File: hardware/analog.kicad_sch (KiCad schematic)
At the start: 23 parts

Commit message: updated trig
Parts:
- renumbered C5 to C?, C6 to C?, C4 to C?, C3 to C?

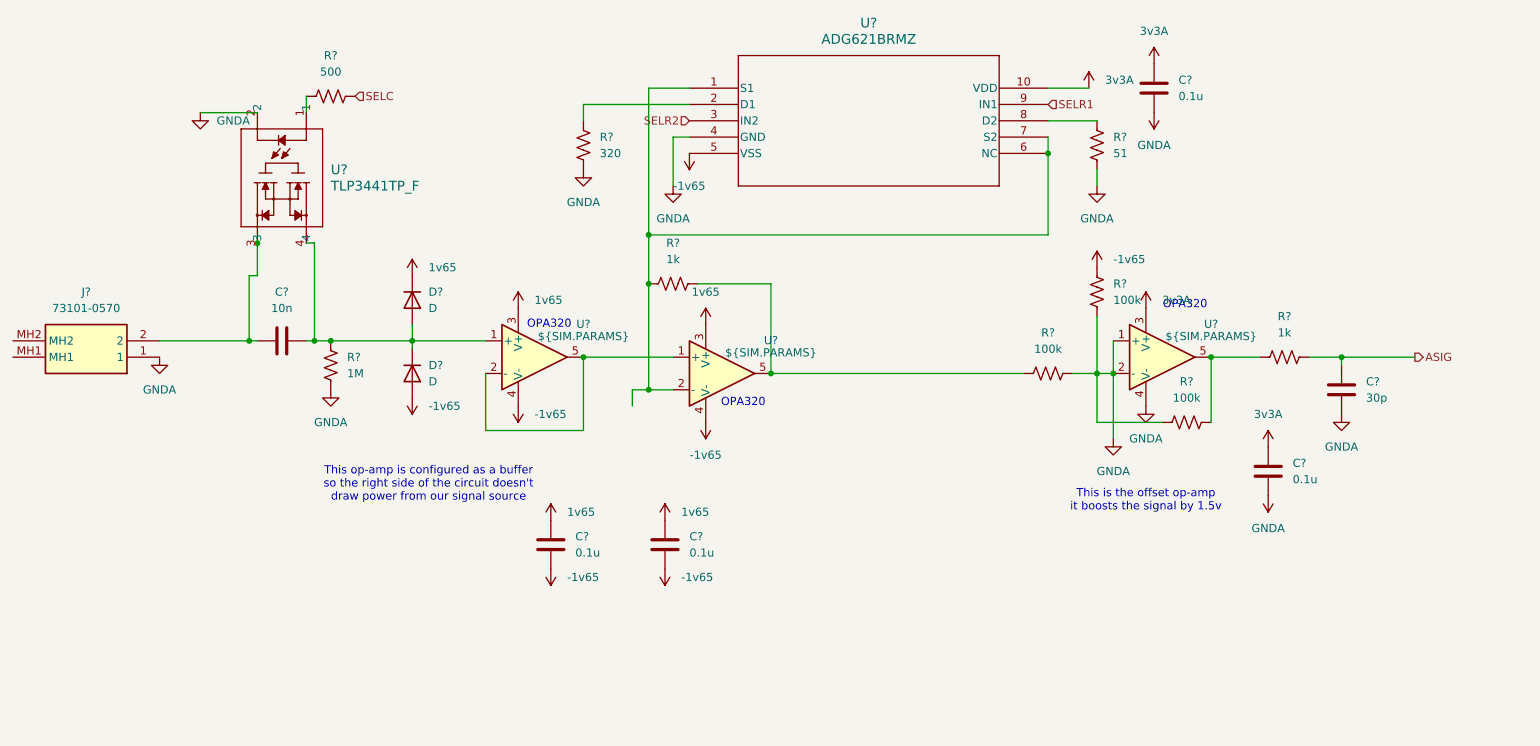
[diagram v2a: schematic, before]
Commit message: feat(hardware): Cleanup schematic, replace offset stage with non-inverting op amp, add neopixel LED
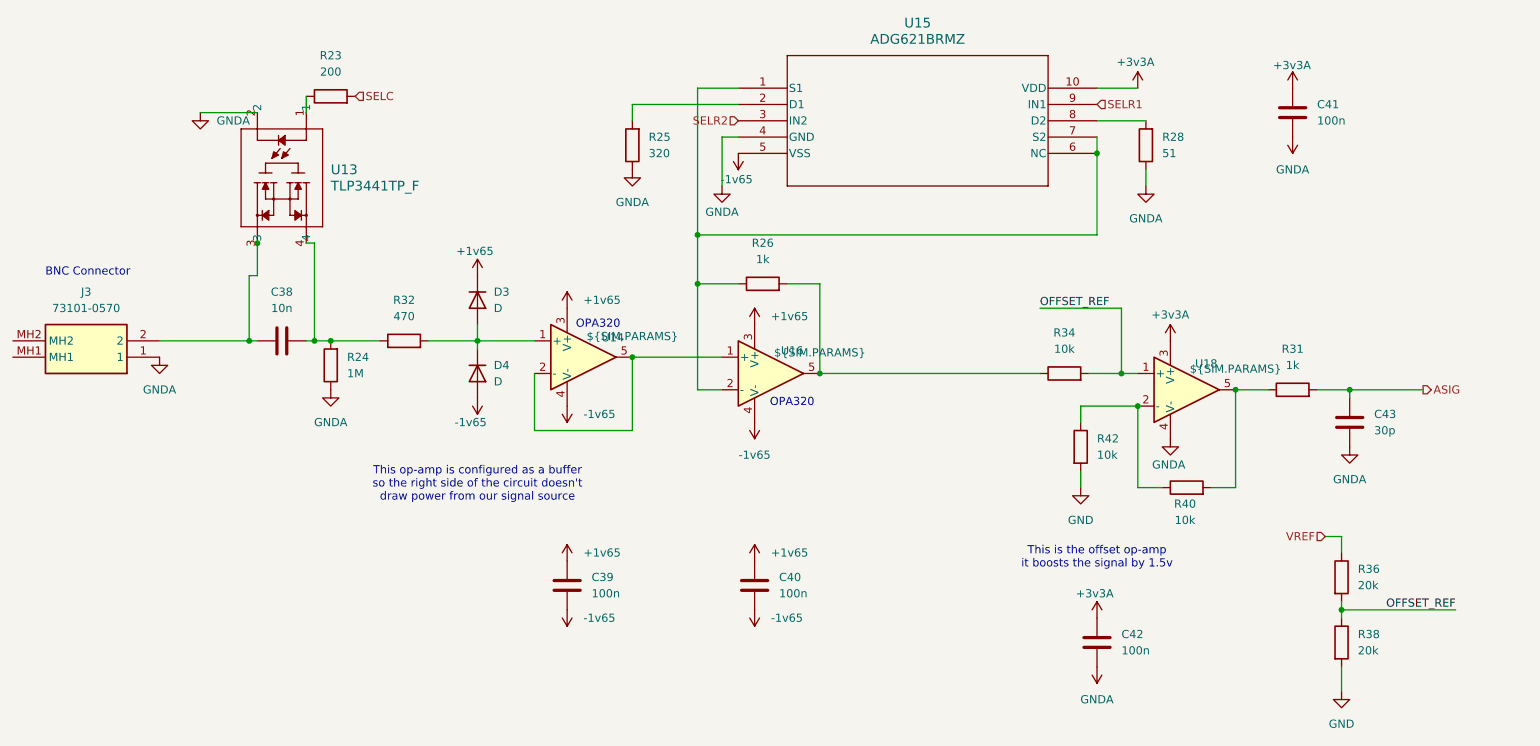
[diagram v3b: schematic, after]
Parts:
- removed R? (x3): 100k, symbol Device:R_US
- removed U?: ${SIM.PARAMS}, symbol Simulation_SPICE:OPAMP
- added R32: 470, symbol Device:R
- added R34, R40, R42: 10k, symbol Device:R
- added R36, R38: 20k, symbol Device:R
- added U18: ${SIM.PARAMS}, symbol Simulation_SPICE:OPAMP
- C39, C40, C41, C42: renamed from C?; value 0.1u -> 100n
- R23: renamed from R?; value 500 -> 200; symbol Device:R_US -> Device:R
- R24, R25, R26, R28, R31: renamed from R?; symbol Device:R_US -> Device:R
- gave numbers to parts that had none: 9
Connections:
- net GNDA: now also U18.4 (V-)
- net at D3.2 (A), D4.1 (K), U14.1 (+): now also R32.2; no longer C38.2, R24.2
- net at R26.2, U16.5: now also R34.1
- net at R31.1: now also R40.2, U18.5
- net 1v65 renamed +1v65
- net 3v3A renamed +3v3A
- net +3v3A: now also U18.3 (V+)
- new net: R40.1, R42.1, U18.2 (-)
- new net: C38.2, R24.2, R32.1
- new net GND: R38.2, R42.2
- new net OFFSET_REF: R34.2, R36.2, R38.1, U18.1 (+)
- new net VREF: R36.1
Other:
- note added: "BNC Connector"
- moved on the sheet: C39, C40, C41, C42, C43, D3, D4, U14, U15, U16
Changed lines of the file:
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@@
 	(generator "eeschema")
 	(generator_version "9.0")
-	(paper "A4")
+	(paper "USLetter")
 	(title_block
 		(title "analog frontend")

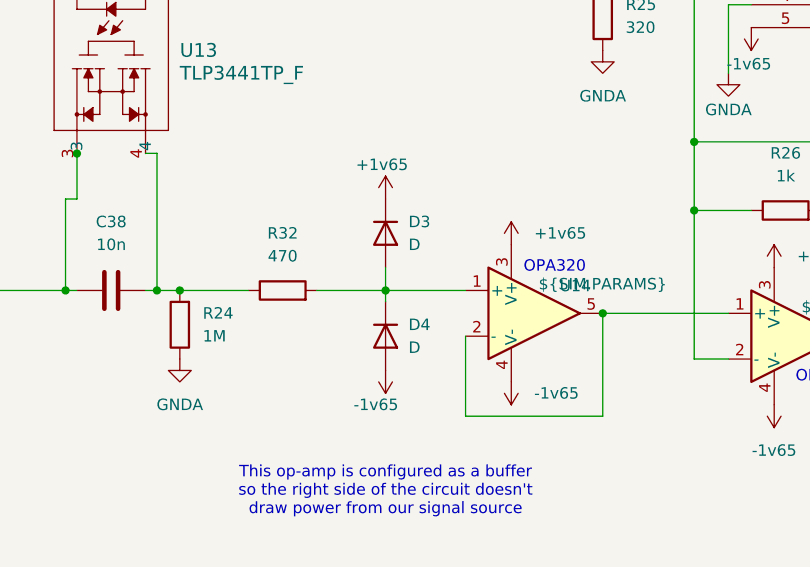
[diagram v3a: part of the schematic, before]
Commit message: feat(hardware): Add charge pump over-voltage protection
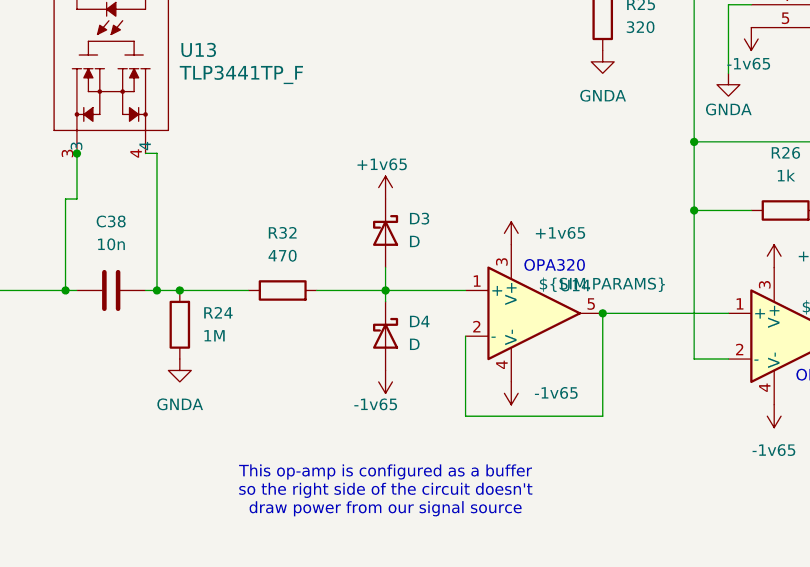
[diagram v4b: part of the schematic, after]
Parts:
- D3, D4: symbol Device:D -> Device:D_Schottky

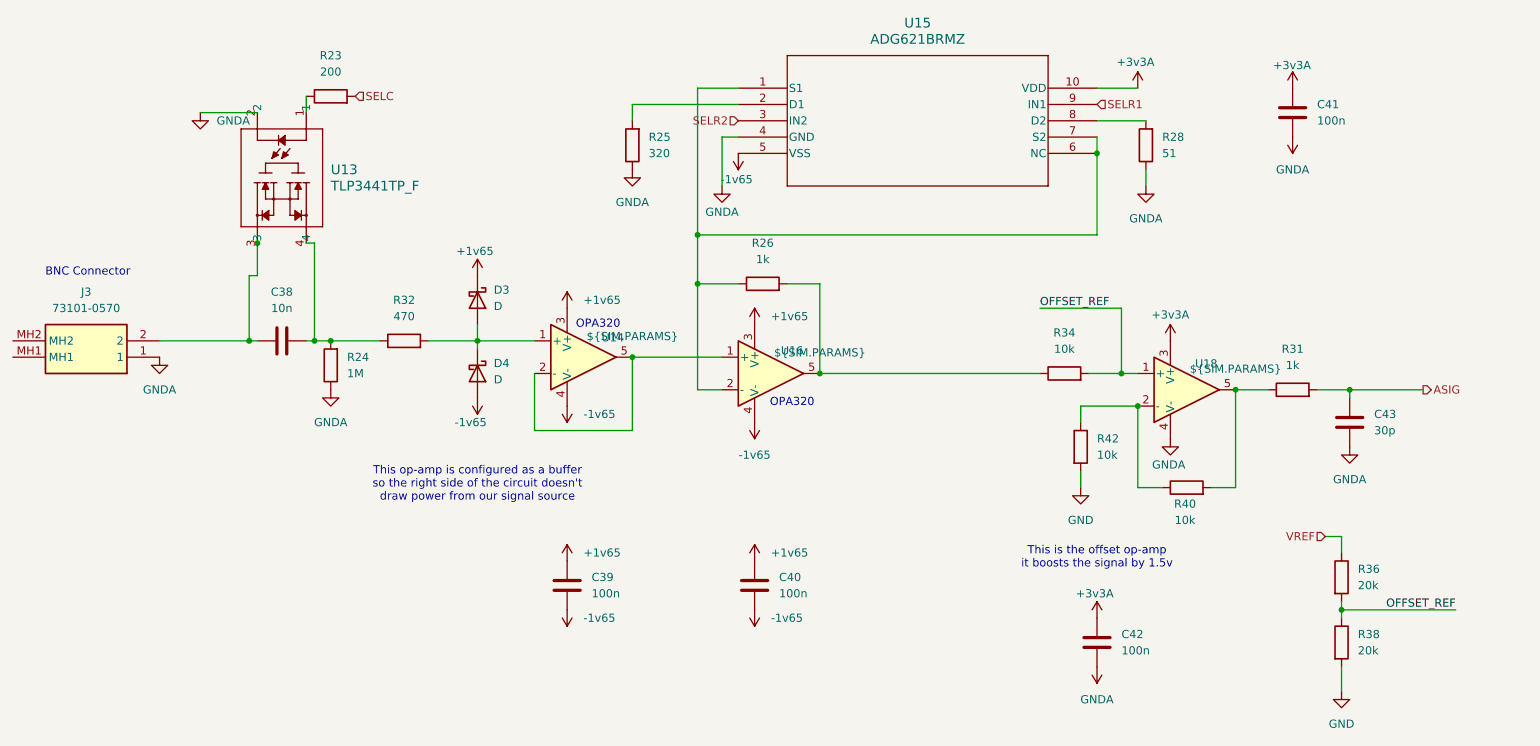
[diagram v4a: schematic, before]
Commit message: fix(hardware): Make power rail net naming consistent
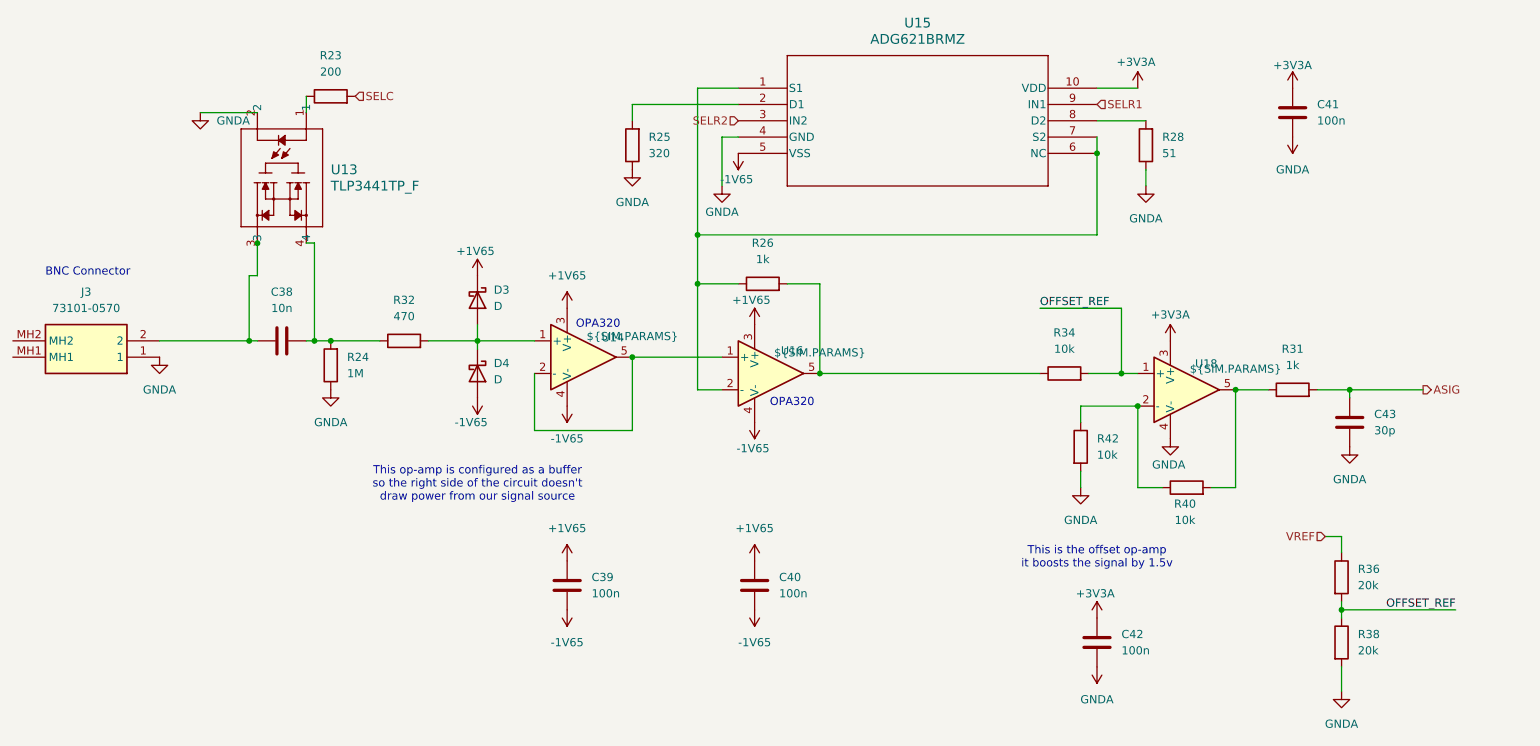
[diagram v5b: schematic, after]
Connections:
- net GND is gone; now on net GNDA: R38.2, R42.2
- net +1v65 renamed +1V65
- net +3v3A renamed +3V3A
- net -1v65 renamed -1V65

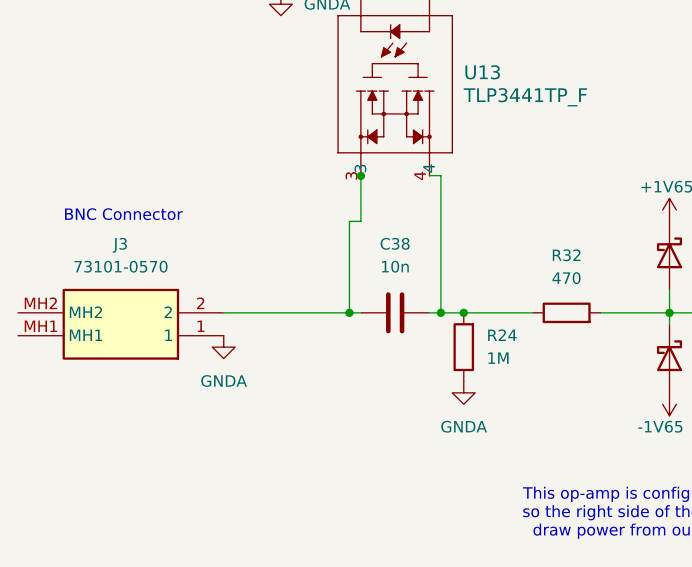
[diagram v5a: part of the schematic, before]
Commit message: feat(hardware): Add zero ohm resistor before analog input
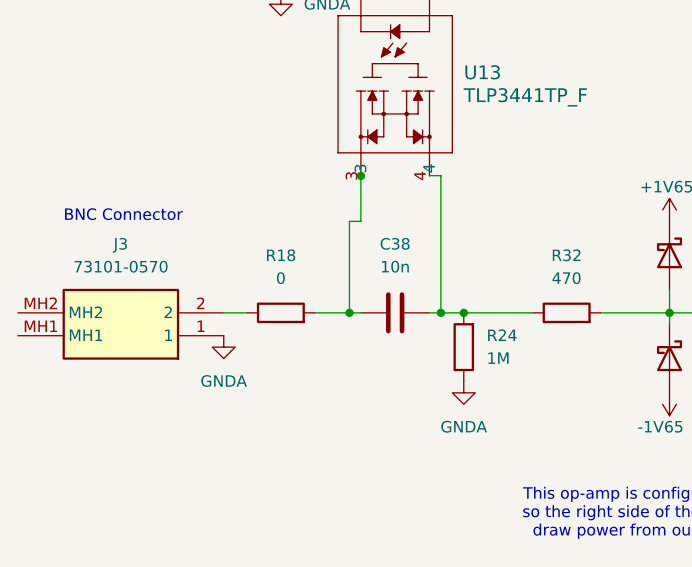
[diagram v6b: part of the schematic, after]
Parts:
- added R18: 0, symbol Device:R
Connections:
- net at C38.1, U13.3: now also R18.2; no longer J3.2
- new net: J3.2, R18.1

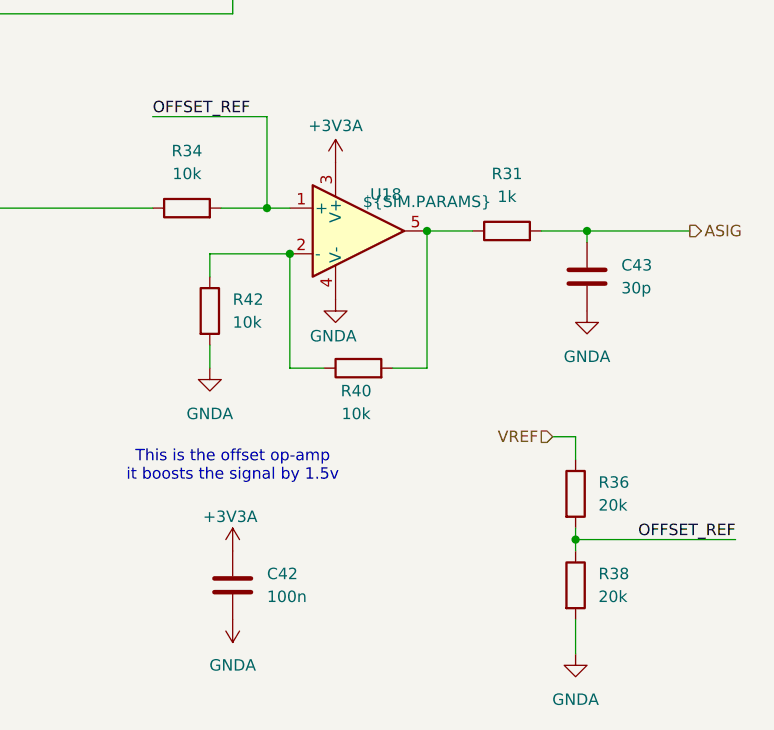
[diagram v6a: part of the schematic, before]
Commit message: added footprints
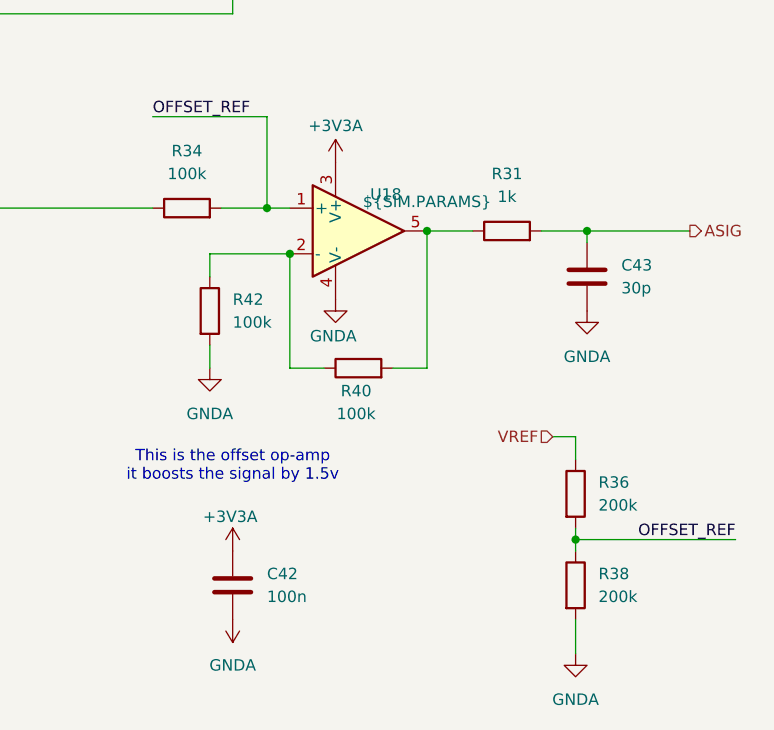
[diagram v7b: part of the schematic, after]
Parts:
- C38, C39, C40, C41, C42, C43: footprint (none) -> Capacitor_SMD:C_0402_1005Metric
- D3, D4: footprint (none) -> Diode_SMD:D_SOD-123
- J3: footprint 731010570 -> BNC:731010570
- R18, R23, R26, R31, R32: footprint (none) -> Resistor_SMD:R_0402_1005Metric
- R24, R25, R28: footprint (none) -> Resistor_SMD:R_0603_1608Metric
- R34, R40, R42: value 10k -> 100k; footprint (none) -> Resistor_SMD:R_0402_1005Metric
- R36, R38: value 20k -> 200k; footprint (none) -> Resistor_SMD:R_0402_1005Metric
- U13: footprint VSON4_TOS -> TLP3441:VSON4_TOS
- U14, U16, U18: footprint (none) -> OPA320:DBV5
- U15: footprint RM_10_ADI -> ADG621BRMZ:RM_10_ADI
